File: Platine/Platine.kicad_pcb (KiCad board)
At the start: 2 copper layers, 8 parts

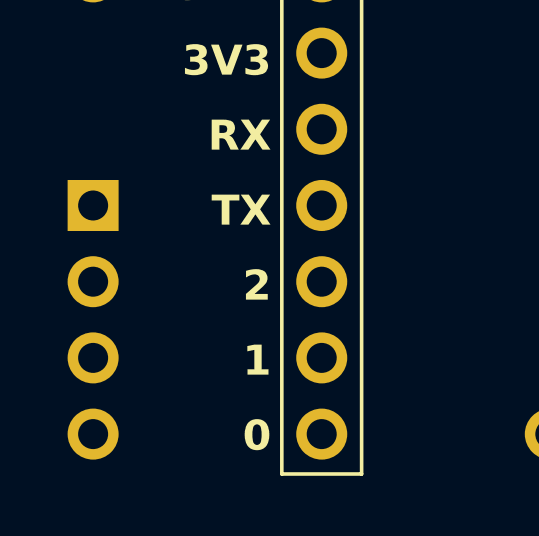
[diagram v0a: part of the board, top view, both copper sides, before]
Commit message: Platine hat alle Netze
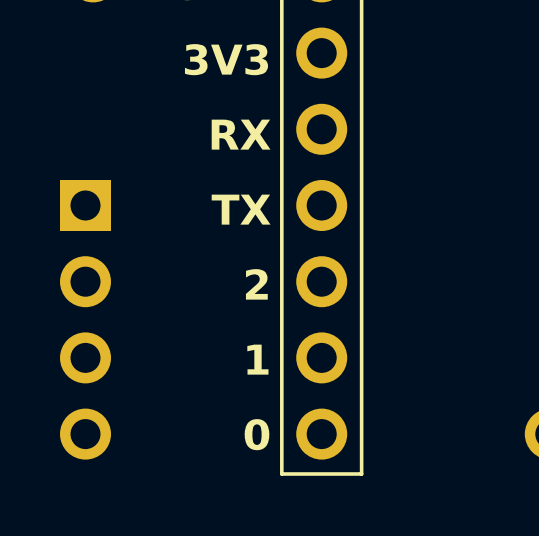
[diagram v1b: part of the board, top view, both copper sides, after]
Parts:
- moved Fan2 33.3 mm to (98.8, 142.2)
- moved Fan1 33.0 mm to (132.1, 142.2)
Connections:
- BME280 pad 3: (no net) -> SCL
- BME280 pad 4: (no net) -> SDA
- ESP32-C3 pad 5: (no net) -> SCL
- ESP32-C3 pad 6: (no net) -> SDA
- ESP32-C3 pad 7: (no net) -> Fan_Tacho
- ESP32-C3 pad 8: (no net) -> Fan_PWM
- ESP32-C3 pad 6: (no net) -> Fan_Relais
- ESP32-C3 pad 7: (no net) -> Pump_Relais
- Fan1 pad 1: (no net) -> Fan_Tacho
- Fan1 pad 2: (no net) -> Fan_PWM
- Fan2 pad 2: (no net) -> Fan_PWM
- FanRelais pad 1: (no net) -> Fan_Relais
- PumpRelais pad 1: (no net) -> Pump_Relais
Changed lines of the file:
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@@
 	(net 3 "5V")
 	(net 4 "12V")
+	(net 5 "Fan_Relais")
+	(net 6 "Pump_Relais")
+	(net 7 "SCL")
+	(net 8 "SDA")
+	(net 9 "Fan_Tacho")
+	(net 10 "Fan_PWM")
 	(footprint "Connector_PinSocket_2.54mm:PinSocket_1x08_P2.54mm_Vertical"
 		(layer "F.Cu")
@@
 			(layers "*.Cu" "*.Mask")
 			(remove_unused_layers no)
+			(net 7 "SCL")
 		)
 		(pad "6" thru_hole circle
@@
 			(layers "*.Cu" "*.Mask")
 			(remove_unused_layers no)
+			(net 8 "SDA")
 		)
 		(pad "7" thru_hole circle
@@
 			(layers "*.Cu" "*.Mask")
 			(remove_unused_layers no)
+			(net 9 "Fan_Tacho")
 		)
 		(pad "8" thru_hole circle
@@
 			(layers "*.Cu" "*.Mask")
 			(remove_unused_layers no)
+			(net 10 "Fan_PWM")
 		)
 		(embedded_fonts no)
@@
 			(layers "*.Cu" "*.Mask")
 			(remove_unused_layers no)
+			(net 5 "Fan_Relais")
 		)
 		(pad "7" thru_hole circle
@@
 			(layers "*.Cu" "*.Mask")
 			(remove_unused_layers no)
+			(net 6 "Pump_Relais")
 		)
 		(pad "8" thru_hole circle
@@
 			(layers "*.Cu" "*.Mask")
 			(remove_unused_layers no)
+			(net 6 "Pump_Relais")
 		)
 		(pad "2" thru_hole circle
@@
 	(footprint "Connector_PinHeader_2.54mm:PinHeader_1x04_P2.54mm_Vertical"
 		(layer "B.Cu")
-		(at 132.08 142.24 180)
+		(at 98.806 142.24 180)
 		(descr "Through hole straight pin header, 1x04, 2.54mm pitch, single row")
 		(tags "Through hole pin header THT 1x04 2.54mm single row")
@@
 			(layers "*.Cu" "*.Mask")
 			(remove_unused_layers no)
+			(net 10 "Fan_PWM")
 		)
 		(pad "3" thru_hole circle
@@
 			(layers "*.Cu" "*.Mask")
 			(remove_unused_layers no)
+			(net 5 "Fan_Relais")
 		)
 		(pad "2" thru_hole circle
@@
 	(footprint "Connector_PinHeader_2.54mm:PinHeader_1x04_P2.54mm_Vertical"
 		(layer "B.Cu")
-		(at 99.06 142.24 180)
+		(at 132.08 142.24 180)
 		(descr "Through hole straight pin header, 1x04, 2.54mm pitch, single row")
 		(tags "Through hole pin header THT 1x04 2.54mm single row")
@@
 			(layers "*.Cu" "*.Mask")
 			(remove_unused_layers no)
+			(net 9 "Fan_Tacho")
 		)
 		(pad "2" thru_hole circle
@@
 			(layers "*.Cu" "*.Mask")
 			(remove_unused_layers no)
+			(net 10 "Fan_PWM")
 		)
 		(pad "3" thru_hole circle
@@
 			(layers "*.Cu" "*.Mask")
 			(remove_unused_layers no)
+			(net 7 "SCL")
 		)
 		(pad "4" thru_hole circle
@@
 			(layers "*.Cu" "*.Mask")
 			(remove_unused_layers no)
+			(net 8 "SDA")
 		)
 		(embedded_fonts no)
@@
 	)
 	(gr_text "GND"
-		(at 97.5 150.5 0)
+		(at 130.52 150.5 0)
 		(layer "B.SilkS")
 		(effects
@@
 	)
 	(gr_text "Tacho"
-		(at 130.5 142.5 0)
+		(at 97.226 142.5 0)
 		(layer "B.SilkS")
 		(effects
@@
 	)
 	(gr_text "VCC"
-		(at 97.5 148 0)
+		(at 130.52 148 0)
 		(layer "B.SilkS")
 		(effects
@@
 	)
 	(gr_text "Tacho"
-		(at 97.5 142.5 0)
+		(at 130.52 142.5 0)
 		(layer "B.SilkS")
 		(effects
@@
 	)
 	(gr_text "PWM"
-		(at 130.5 145 0)
+		(at 97.226 145 0)
 		(layer "B.SilkS")
 		(effects
@@
 	)
 	(gr_text "VCC"
-		(at 130.5 148 0)
+		(at 97.226 148 0)
 		(layer "B.SilkS")
 		(effects
@@
 	)
 	(gr_text "GND"
-		(at 130.5 150.5 0)
+		(at 97.226 150.5 0)
 		(layer "B.SilkS")
 		(effects
@@
 	)
 	(gr_text "PWM"
-		(at 97.5 145 0)
+		(at 130.52 145 0)
 		(layer "B.SilkS")
 		(effects

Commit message: Platine finalisiert
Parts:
- ESP32-C3: value ESP32-C3 right -> ESP32-C3 left
- ESP32-C3: value ESP32-C3 left -> ESP32-C3 right
- Fan1: renamed from Fan2; value Fan 2 -> Fan 1
- Fan2: renamed from Fan1; value Fan 1 -> Fan 2
- moved FanRelais 27.9 mm to (99.1, 157.5)
- moved PumpRelais 27.9 mm to (132.1, 157.5)
- moved 12V 25.5 mm to (114.3, 124.5), turned to 180 degrees
- moved ESP32-C3 25.1 mm to (106.7, 149.9), turned to 180 degrees
- moved ESP32-C3 25.1 mm to (124.5, 149.9), turned to 180 degrees
- moved BME280 21.0 mm to (119.3, 135.3)
- moved Fan1 10.2 mm to (99.1, 132.1), turned to 0 degrees
- moved Fan2 10.2 mm to (132.1, 132.1), turned to 0 degrees
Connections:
- BME280 pad 1: GND -> 3V3
- BME280 pad 2: 3V3 -> GND
- Fan1 pad 1: (no net) -> Fan_Tacho
- Fan2 pad 1: Fan_Tacho -> (no net)
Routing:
- net GND: track 0.00 -> 175.5 mm, vias 0 -> 2
- net 5V: track 0.00 -> 43.2 mm
- net Fan_Relais: track 0.00 -> 38.3 mm, vias 0 -> 2
- net Fan_PWM: track 0.00 -> 35.6 mm
- net 12V: track 0.00 -> 33.0 mm
- net Pump_Relais: track 0.00 -> 29.0 mm
- net 3V3: track 0.00 -> 13.1 mm
- net SCL: track 0.00 -> 9.36 mm
- net Fan_Tacho: track 0.00 -> 8.67 mm
- net SDA: track 0.00 -> 5.77 mm
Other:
- board outline added: 43.2 x 50.8 mm

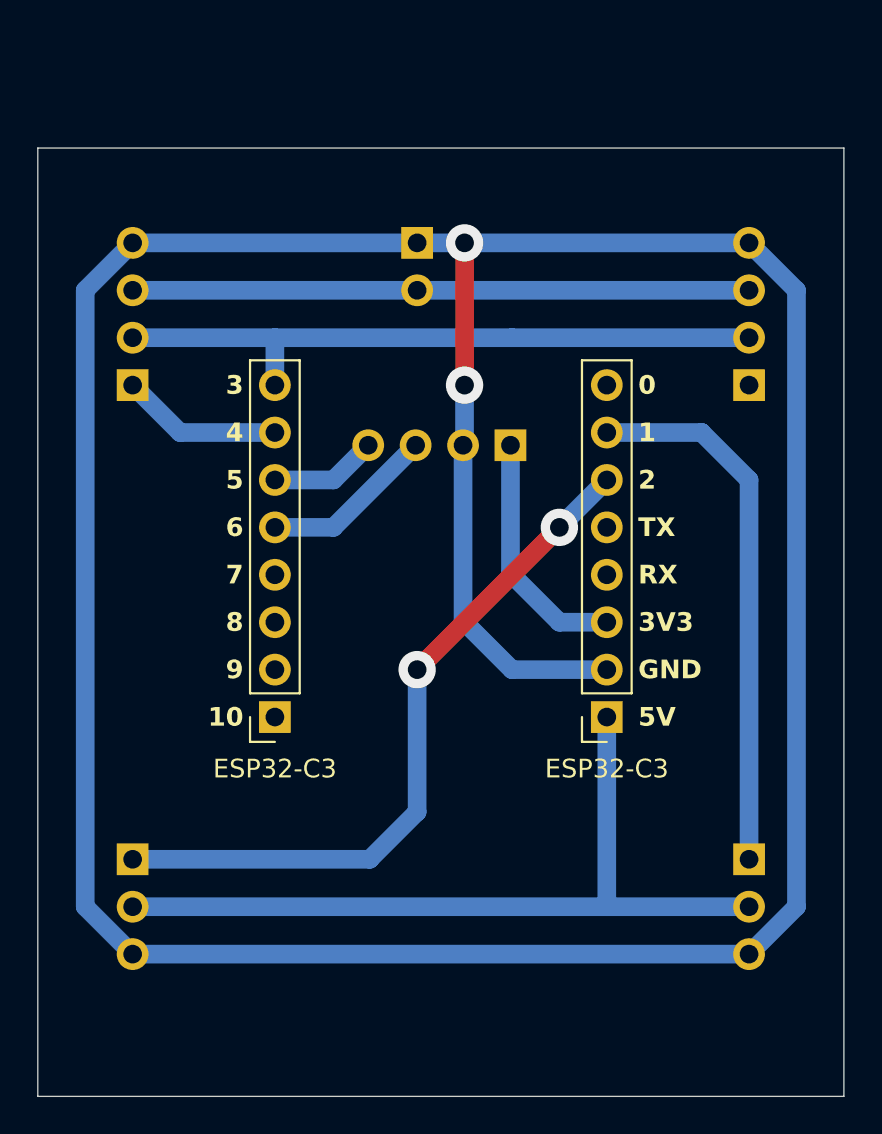
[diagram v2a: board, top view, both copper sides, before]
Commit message: vertauschte PWM und Tacho Pins korrigiert
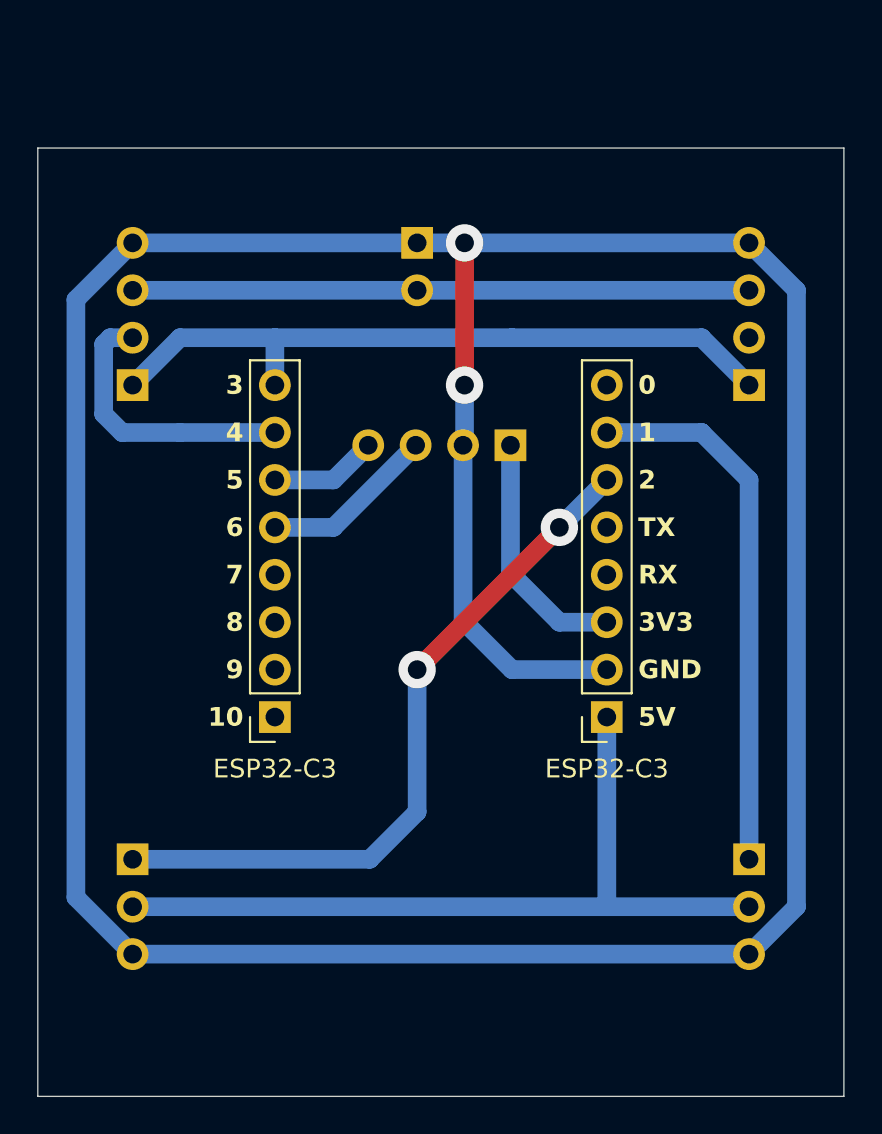
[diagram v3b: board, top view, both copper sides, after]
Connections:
- Fan1 pad 1: Fan_Tacho -> Fan_PWM
- Fan1 pad 2: Fan_PWM -> Fan_Tacho
- Fan2 pad 1: (no net) -> Fan_PWM
- Fan2 pad 2: Fan_PWM -> (no net)
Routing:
- net Fan_Tacho: track 8.67 -> 15.0 mm
- net Fan_PWM: track 35.6 -> 37.7 mm
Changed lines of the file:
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@@
 			(layers "*.Cu" "*.Mask")
 			(remove_unused_layers no)
-			(net 9 "Fan_Tacho")
+			(net 10 "Fan_PWM")
 		)
 		(pad "2" thru_hole circle
@@
 			(layers "*.Cu" "*.Mask")
 			(remove_unused_layers no)
-			(net 10 "Fan_PWM")
+			(net 9 "Fan_Tacho")
 		)
 		(pad "3" thru_hole circle
@@
 			(layers "*.Cu" "*.Mask")
 			(remove_unused_layers no)
+			(net 10 "Fan_PWM")
 		)
 		(pad "2" thru_hole circle
@@
 			(layers "*.Cu" "*.Mask")
 			(remove_unused_layers no)
-			(net 10 "Fan_PWM")
 		)
 		(pad "3" thru_hole circle
@@
 	)
 	(gr_text "Tacho"
-		(at 101 132.08 0)
+		(at 101 129.54 0)
 		(layer "B.SilkS")
 		(effects
@@
 	)
 	(gr_text "Tacho"
-		(at 130.4 132.08 0)
+		(at 130.4 129.54 0)
 		(layer "B.SilkS")
 		(effects
@@
 	)
 	(gr_text "PWM"
-		(at 101 129.54 0)
+		(at 101 132.08 0)
 		(layer "B.SilkS")
 		(effects
@@
 	)
 	(gr_text "PWM"
-		(at 130.4 129.54 0)
+		(at 130.4 132.08 0)
 		(layer "B.SilkS")
 		(effects
@@
 	)
 	(segment
+		(start 99.06 124.459999)
+		(end 96.021 127.498999)
+		(width 1)
+		(layer "B.Cu")
+		(net 1)
+	)
+	(segment
 		(start 114.3 124.46)
 		(end 132.08 124.46)
@@
 	)
 	(segment
-		(start 96.52 160.02)
-		(end 99.06 162.56)
-		(width 1)
-		(layer "B.Cu")
-		(net 1)
-	)
-	(segment
 		(start 116.76 135.300119)
 		(end 116.76 144.7)
@@
 	)
 	(segment
-		(start 99.06 124.459999)
-		(end 96.52 127)
+		(start 96.021 127.498999)
+		(end 96.021 159.521)
+		(width 1)
+		(layer "B.Cu")
+		(net 1)
+	)
+	(segment
+		(start 96.021 159.521)
+		(end 99.06 162.56)
 		(width 1)
 		(layer "B.Cu")
@@
 		(start 119.380002 147.320002)
 		(end 124.459996 147.320002)
-		(width 1)
-		(layer "B.Cu")
-		(net 1)
-	)
-	(segment
-		(start 96.52 127)
-		(end 96.52 160.02)
 		(width 1)
 		(layer "B.Cu")
@@
 	)
 	(segment
-		(start 106.679996 134.620002)
+		(start 97.857919 129.539999)
+		(end 97.509 129.888918)
+		(width 1)
+		(layer "B.Cu")
+		(net 9)
+	)
+	(segment
+		(start 101.600001 134.62)
 		(end 101.600003 134.620002)
 		(width 1)
@@
 	)
 	(segment
+		(start 97.509 133.630999)
+		(end 98.498001 134.62)
+		(width 1)
+		(layer "B.Cu")
+		(net 9)
+	)
+	(segment
 		(start 101.600003 134.620002)
-		(end 99.06 132.079999)
+		(end 106.679996 134.620002)
 		(width 1)
 		(layer "B.Cu")
@@
 	)
 	(segment
+		(start 97.509 129.888918)
+		(end 97.509 133.630999)
+		(width 1)
+		(layer "B.Cu")
+		(net 9)
+	)
+	(segment
 		(start 99.06 129.539999)
-		(end 106.68 129.539999)
+		(end 97.857919 129.539999)
+		(width 1)
+		(layer "B.Cu")
+		(net 9)
+	)
+	(segment
+		(start 98.498001 134.62)
+		(end 101.600001 134.62)
+		(width 1)
+		(layer "B.Cu")
+		(net 9)
+	)
+	(segment
+		(start 106.68 129.539999)
+		(end 119.379999 129.539999)
 		(width 1)
 		(layer "B.Cu")
@@
 	)
 	(segment
-		(start 119.38 129.54)
-		(end 132.08 129.54)
+		(start 99.06 132.079999)
+		(end 101.6 129.539999)
 		(width 1)
 		(layer "B.Cu")
@@
 	)
 	(segment
+		(start 119.38 129.54)
+		(end 129.54 129.54)
+		(width 1)
+		(layer "B.Cu")
+		(net 10)
+	)
+	(segment
 		(start 119.379999 129.539999)
 		(end 119.38 129.54)
@@
 	)
 	(segment
-		(start 106.68 129.539999)
-		(end 119.379999 129.539999)
+		(start 129.54 129.54)
+		(end 132.08 132.08)
+		(width 1)
+		(layer "B.Cu")
+		(net 10)
+	)
+	(segment
+		(start 101.6 129.539999)
+		(end 106.68 129.539999)
 		(width 1)
 		(layer "B.Cu")
@@
 	)
 	(group ""
+		(members "12711890-d8e4-4f99-8f92-0b0415eddb56" "76102ebb-488d-4a41-93a8-e3627f84bd04"
+			"765be9fa-2022-47a0-8445-4ce5b56ee83c" "a683afa1-6fd0-498c-954c-b3d803b01688"
+			"a8d2384a-fc18-4da2-b025-db46275cd7b9"
+		)
+	)
+	(group ""
 		(members "432e5564-c7ad-4a1e-8f28-841f1c12c3b3" "4ae81eda-47d6-4cbe-86a5-c9af619c1def"
 			"9e64b485-1f83-4d9b-8ec5-0c80630efd45" "a05c026c-7f45-4f01-8d6b-b4373faf7592"
@@
 		)
 	)
-	(group ""
-		(members "12711890-d8e4-4f99-8f92-0b0415eddb56" "76102ebb-488d-4a41-93a8-e3627f84bd04"
-			"765be9fa-2022-47a0-8445-4ce5b56ee83c" "a683afa1-6fd0-498c-954c-b3d803b01688"
-			"a8d2384a-fc18-4da2-b025-db46275cd7b9"
-		)
-	)
